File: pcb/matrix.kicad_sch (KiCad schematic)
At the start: 122 parts, among them SW1 SW_Push, SW10 SW_Push, SW11 SW_Push, SW12 SW_Push, SW13 SW_Push, SW14 SW_Push, SW15 SW_Push, SW16 SW_Push, SW17 SW_Push, SW18 SW_Push, SW19 SW_Push, SW2 SW_Push, SW20 SW_Push, SW21 SW_Push, SW22 SW_Push, SW23 SW_Push, SW24 SW_Push, SW25 SW_Push, SW26 SW_Push, SW27 SW_Push, SW28 SW_Push, SW29 SW_Push, SW3 SW_Push, SW30 SW_Push, SW31 SW_Push, SW32 SW_Push, SW33 SW_Push, SW34 SW_Push, SW35 SW_Push, SW36 SW_Push, SW37 SW_Push, SW38 SW_Push, SW39 SW_Push, SW4 SW_Push, SW40 SW_Push, SW41 SW_Push, SW42 SW_Push, SW43 SW_Push, SW44 SW_Push, SW45 SW_Push, SW46 SW_Push, SW47 SW_Push, SW48 SW_Push, SW49 SW_Push, SW5 SW_Push, SW50 SW_Push, SW51 SW_Push, SW52 SW_Push, SW53 SW_Push, SW54 SW_Push, SW55 SW_Push, SW56 SW_Push, SW57 SW_Push, SW58 SW_Push, SW59 SW_Push, SW6 SW_Push, SW60 SW_Push, SW61 SW_Push, SW7 SW_Push, SW8 SW_Push, SW9 SW_Push

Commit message: Finish board schematic
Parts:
- D1, D10, D11, D12, D13, D14, D15, D16, D17, D18, D19, D2, D20, D21, D22, D23, D24, D25, D26, D27, D28, D29, D3, D30, D31, D32, D33, D34, D35, D36, D37, D38, D39, D4, D40, D41, D42, D43, D44, D45, D46, D47, D48, D49, D5, D50, D51, D52, D53, D54, D55, D56, D57, D58, D59, D6, D60, D61, D7, D8, D9: footprint (none) -> Diode_SMD:D_SOD-123
- SW1, SW10, SW11, SW12, SW13, SW16, SW17, SW18, SW19, SW2, SW20, SW21, SW22, SW23, SW24, SW25, SW26, SW27, SW3, SW30, SW31, SW32, SW33, SW34, SW35, SW36, SW37, SW38, SW39, SW4, SW40, SW43, SW44, SW45, SW46, SW47, SW48, SW49, SW5, SW50, SW51, SW52, SW6, SW7, SW8, SW9: footprint (none) -> ai03_MX:MX-Solderable-1U
- SW14: footprint (none) -> ai03_MX:MX-Solderable-2U
- SW15, SW28: footprint (none) -> ai03_MX:MX-Solderable-1.5U
- SW29: footprint (none) -> ai03_MX:MX-Solderable-1.75U
- SW41, SW42: footprint (none) -> ai03_MX:MX-Solderable-2.25U
- SW53: footprint (none) -> ai03_MX:MX-Solderable-2.75U
- SW54, SW55, SW56, SW58, SW59, SW60, SW61: footprint (none) -> ai03_MX:MX-Solderable-1.25U
- SW57: footprint (none) -> ai03_MX:MX-Solderable-6.25U

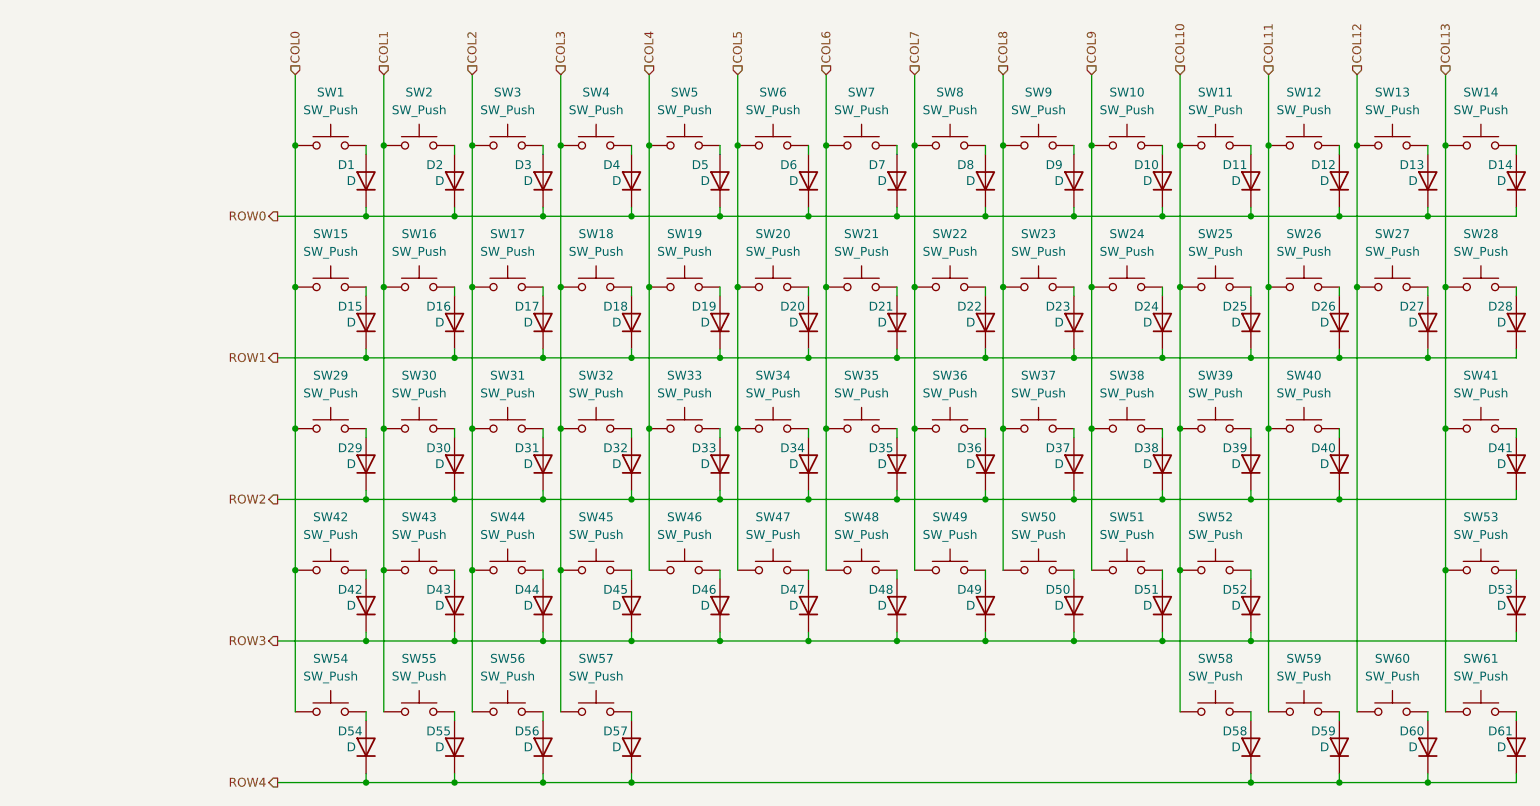
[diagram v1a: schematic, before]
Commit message: Reverse diodes on keyboard matrix
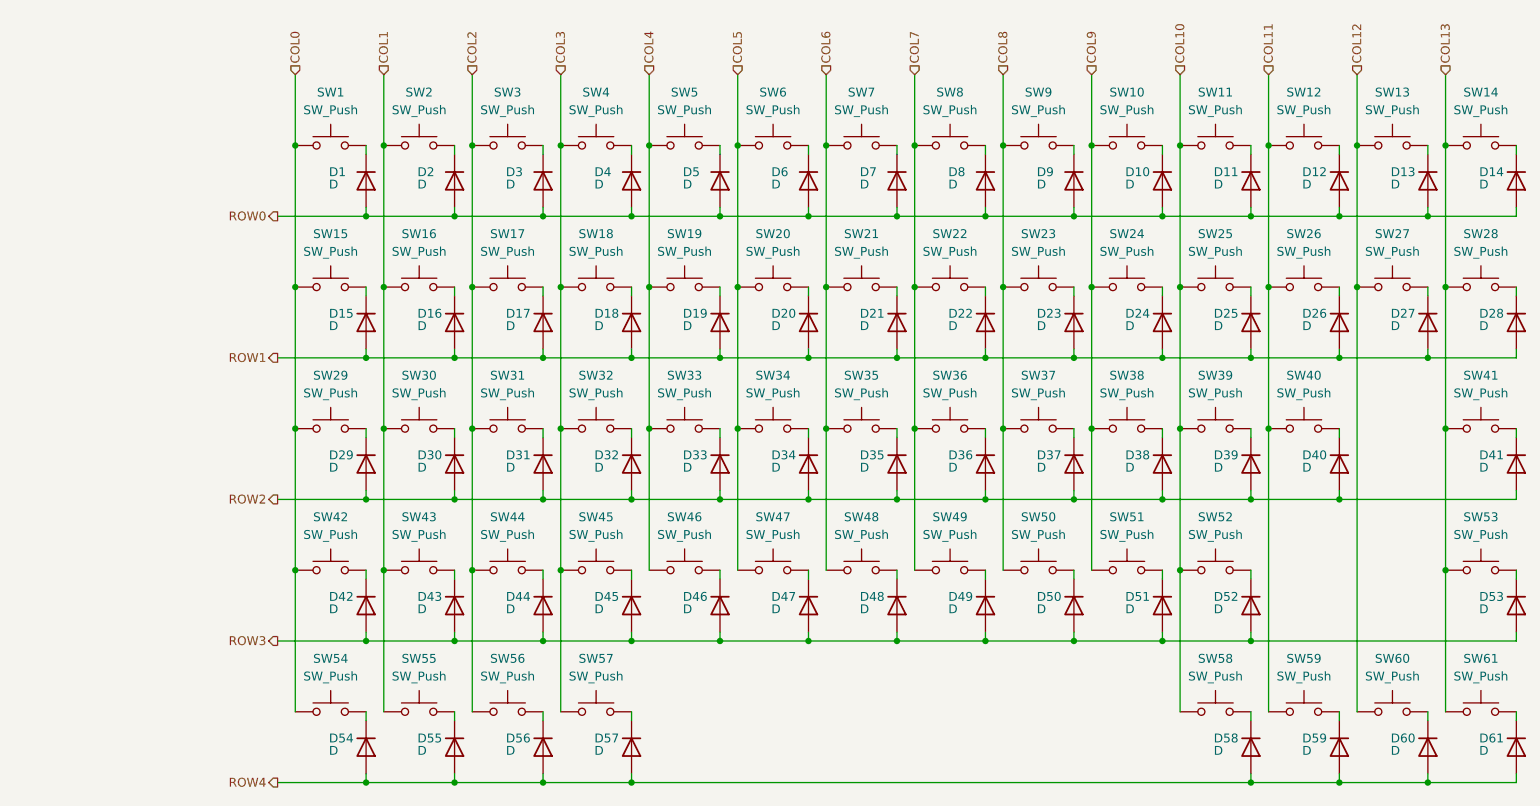
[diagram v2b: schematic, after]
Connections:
- net ROW0: now also D1.2 (A), D10.2 (A), D11.2 (A), D12.2 (A), D13.2 (A), D14.2 (A), D2.2 (A), D3.2 (A), D4.2 (A), D5.2 (A), D6.2 (A), D7.2 (A), D8.2 (A), D9.2 (A); no longer D1.1 (K), D10.1 (K), D11.1 (K), D12.1 (K), D13.1 (K), D14.1 (K), D2.1 (K), D3.1 (K), D4.1 (K), D5.1 (K), D6.1 (K), D7.1 (K), D8.1 (K), D9.1 (K)
- net ROW1: now also D15.2 (A), D16.2 (A), D17.2 (A), D18.2 (A), D19.2 (A), D20.2 (A), D21.2 (A), D22.2 (A), D23.2 (A), D24.2 (A), D25.2 (A), D26.2 (A), D27.2 (A), D28.2 (A); no longer D15.1 (K), D16.1 (K), D17.1 (K), D18.1 (K), D19.1 (K), D20.1 (K), D21.1 (K), D22.1 (K), D23.1 (K), D24.1 (K), D25.1 (K), D26.1 (K), D27.1 (K), D28.1 (K)
- net ROW2: now also D29.2 (A), D30.2 (A), D31.2 (A), D32.2 (A), D33.2 (A), D34.2 (A), D35.2 (A), D36.2 (A), D37.2 (A), D38.2 (A), D39.2 (A), D40.2 (A), D41.2 (A); no longer D29.1 (K), D30.1 (K), D31.1 (K), D32.1 (K), D33.1 (K), D34.1 (K), D35.1 (K), D36.1 (K), D37.1 (K), D38.1 (K), D39.1 (K), D40.1 (K), D41.1 (K)
- net ROW3: now also D42.2 (A), D43.2 (A), D44.2 (A), D45.2 (A), D46.2 (A), D47.2 (A), D48.2 (A), D49.2 (A), D50.2 (A), D51.2 (A), D52.2 (A), D53.2 (A); no longer D42.1 (K), D43.1 (K), D44.1 (K), D45.1 (K), D46.1 (K), D47.1 (K), D48.1 (K), D49.1 (K), D50.1 (K), D51.1 (K), D52.1 (K), D53.1 (K)
- net ROW4: now also D54.2 (A), D55.2 (A), D56.2 (A), D57.2 (A), D58.2 (A), D59.2 (A), D60.2 (A), D61.2 (A); no longer D54.1 (K), D55.1 (K), D56.1 (K), D57.1 (K), D58.1 (K), D59.1 (K), D60.1 (K), D61.1 (K)
- net at SW14.2: now also D14.1 (K); no longer D14.2 (A)
- net at SW36.2: now also D36.1 (K); no longer D36.2 (A)
- net at SW28.2: now also D28.1 (K); no longer D28.2 (A)
- net at SW27.2: now also D27.1 (K); no longer D27.2 (A)
- net at SW44.2: now also D44.1 (K); no longer D44.2 (A)
- net at SW43.2: now also D43.1 (K); no longer D43.2 (A)
- net at SW23.2: now also D23.1 (K); no longer D23.2 (A)
- net at SW15.2: now also D15.1 (K); no longer D15.2 (A)
- net at SW42.2: now also D42.1 (K); no longer D42.2 (A)
- net at SW20.2: now also D20.1 (K); no longer D20.2 (A)
- net at SW33.2: now also D33.1 (K); no longer D33.2 (A)
- net at SW49.2: now also D49.1 (K); no longer D49.2 (A)
- net at SW55.2: now also D55.1 (K); no longer D55.2 (A)
- net at SW10.2: now also D10.1 (K); no longer D10.2 (A)
- net at SW30.2: now also D30.1 (K); no longer D30.2 (A)
- net at SW21.2: now also D21.1 (K); no longer D21.2 (A)
- net at SW19.2: now also D19.1 (K); no longer D19.2 (A)
- net at SW9.2: now also D9.1 (K); no longer D9.2 (A)
- net at SW29.2: now also D29.1 (K); no longer D29.2 (A)
- net at SW53.2: now also D53.1 (K); no longer D53.2 (A)
- net at SW47.2: now also D47.1 (K); no longer D47.2 (A)
- net at SW13.2: now also D13.1 (K); no longer D13.2 (A)
- net at SW60.2: now also D60.1 (K); no longer D60.2 (A)
- net at SW46.2: now also D46.1 (K); no longer D46.2 (A)
- net at SW54.2: now also D54.1 (K); no longer D54.2 (A)
- net at SW35.2: now also D35.1 (K); no longer D35.2 (A)
- net at SW48.2: now also D48.1 (K); no longer D48.2 (A)
- net at SW11.2: now also D11.1 (K); no longer D11.2 (A)
- net at SW39.2: now also D39.1 (K); no longer D39.2 (A)
- net at SW1.2: now also D1.1 (K); no longer D1.2 (A)
- net at SW57.2: now also D57.1 (K); no longer D57.2 (A)
- net at SW59.2: now also D59.1 (K); no longer D59.2 (A)
- net at SW26.2: now also D26.1 (K); no longer D26.2 (A)
- net at SW7.2: now also D7.1 (K); no longer D7.2 (A)
- net at SW25.2: now also D25.1 (K); no longer D25.2 (A)
- net at SW31.2: now also D31.1 (K); no longer D31.2 (A)
- net at SW24.2: now also D24.1 (K); no longer D24.2 (A)
- net at SW2.2: now also D2.1 (K); no longer D2.2 (A)
- net at SW41.2: now also D41.1 (K); no longer D41.2 (A)
- net at SW50.2: now also D50.1 (K); no longer D50.2 (A)
- net at SW5.2: now also D5.1 (K); no longer D5.2 (A)
- net at SW17.2: now also D17.1 (K); no longer D17.2 (A)
- net at SW6.2: now also D6.1 (K); no longer D6.2 (A)
- net at SW8.2: now also D8.1 (K); no longer D8.2 (A)
- net at SW52.2: now also D52.1 (K); no longer D52.2 (A)
- net at SW37.2: now also D37.1 (K); no longer D37.2 (A)
- net at SW4.2: now also D4.1 (K); no longer D4.2 (A)
- net at SW51.2: now also D51.1 (K); no longer D51.2 (A)
- net at SW40.2: now also D40.1 (K); no longer D40.2 (A)
- net at SW18.2: now also D18.1 (K); no longer D18.2 (A)
- net at SW16.2: now also D16.1 (K); no longer D16.2 (A)
- net at SW12.2: now also D12.1 (K); no longer D12.2 (A)
- net at SW38.2: now also D38.1 (K); no longer D38.2 (A)
- net at SW61.2: now also D61.1 (K); no longer D61.2 (A)
- net at SW32.2: now also D32.1 (K); no longer D32.2 (A)
- net at SW34.2: now also D34.1 (K); no longer D34.2 (A)
- net at SW3.2: now also D3.1 (K); no longer D3.2 (A)
- net at SW58.2: now also D58.1 (K); no longer D58.2 (A)
- net at SW56.2: now also D56.1 (K); no longer D56.2 (A)
- net at SW22.2: now also D22.1 (K); no longer D22.2 (A)
- net at SW45.2: now also D45.1 (K); no longer D45.2 (A)

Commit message: Finish and validate schematic
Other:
- title: (none) -> Keyboard Matrix
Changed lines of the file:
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@@
 	(generator_version "9.0")
 	(paper "A4")
+	(title_block
+		(title "Keyboard Matrix")
+		(date "2026-05-05")
+		(rev "A")
+	)
 	(junction
 		(at 173.99 86.36)

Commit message: Finished routing and various fixes
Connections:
- net ROW1: no longer D15.2 (A)
- net ROW2: now also D15.2 (A)
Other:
- note added: "TAB is ROW2"
- moved on the sheet: D1, D15, D29, D42, D54, SW1, SW15, SW29, SW42, SW54
